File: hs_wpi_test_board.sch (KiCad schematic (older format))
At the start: 34 parts

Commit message: add power flags and no connects
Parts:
- gave numbers to parts that had none: 34
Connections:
- no-connect marks 0 -> 17

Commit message: associate footprints
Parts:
- D1, D10, D2, D3, D4, D5, D6, D7, D8, D9: footprint (none) -> LEDs:LED_D5.0mm
- Q1, Q10, Q2, Q3, Q4, Q5, Q6, Q7, Q8, Q9: footprint (none) -> TO_SOT_Packages_THT:TO-92_Inline_Narrow_Oval
- R1, R10, R11, R12, R2, R3, R4, R5, R6, R7, R8, R9: footprint (none) -> Resistors_THT:R_Axial_DIN0207_L6.3mm_D2.5mm_P10.16mm_Horizontal
- SW1: footprint (none) -> Buttons_Switches_THT:SW_PUSH-12mm

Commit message: change footprint for J1
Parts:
- J1: footprint Pin_Headers:Pin_Header_Straight_2x20 -> Pin_Headers:Pin_Header_Straight_2x20_Pitch2.54mm
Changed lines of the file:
@@
 F 0 "J1" H 5850 4950 50  0000 C CNN
 F 1 "Raspberry_Pi_2_3" H 4750 7100 50  0000 C CNN
-F 2 "Pin_Headers:Pin_Header_Straight_2x20" H 6150 7450 50  0001 C CNN
+F 2 "Pin_Headers:Pin_Header_Straight_2x20_Pitch2.54mm" H 6150 7450 50  0001 C CNN
 F 3 "" H 5200 6050 50  0001 C CNN
 	1    5150 6200

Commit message: switch J1 footprint to Connectors:IDC_Header_Straight_40pins
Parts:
- J1: footprint Pin_Headers:Pin_Header_Straight_2x20_Pitch2.54mm -> Connectors:IDC_Header_Straight_40pins
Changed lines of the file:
@@
 F 0 "J1" H 5850 4950 50  0000 C CNN
 F 1 "Raspberry_Pi_2_3" H 4750 7100 50  0000 C CNN
-F 2 "Pin_Headers:Pin_Header_Straight_2x20_Pitch2.54mm" H 6150 7450 50  0001 C CNN
+F 2 "Connectors:IDC_Header_Straight_40pins" H 6150 7450 50  0001 C CNN
 F 3 "" H 5200 6050 50  0001 C CNN
 	1    5150 6200

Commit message: switch to wider footprint for transistors
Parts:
- Q1, Q10, Q2, Q3, Q4, Q5, Q6, Q7, Q8, Q9: footprint TO_SOT_Packages_THT:TO-92_Inline_Narrow_Oval -> TO_SOT_Packages_THT:TO-92_Inline_Wide
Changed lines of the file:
@@
 F 0 "Q9" H 1950 5150 50  0000 L CNN
 F 1 "Q_NPN_EBC" H 1950 5050 50  0000 L CNN
-F 2 "TO_SOT_Packages_THT:TO-92_Inline_Narrow_Oval" H 1950 5200 50  0001 C CNN
+F 2 "TO_SOT_Packages_THT:TO-92_Inline_Wide" H 1950 5200 50  0001 C CNN
 F 3 "" H 1750 5100 50  0001 C CNN
 	1    1750 5100
@@
 F 0 "Q10" H 3200 5150 50  0000 L CNN
 F 1 "Q_NPN_EBC" H 3200 5050 50  0000 L CNN
-F 2 "TO_SOT_Packages_THT:TO-92_Inline_Narrow_Oval" H 3200 5200 50  0001 C CNN
+F 2 "TO_SOT_Packages_THT:TO-92_Inline_Wide" H 3200 5200 50  0001 C CNN
 F 3 "" H 3000 5100 50  0001 C CNN
 	1    3000 5100
@@
 F 0 "Q5" H 1950 3250 50  0000 L CNN
 F 1 "Q_NPN_EBC" H 1950 3150 50  0000 L CNN
-F 2 "TO_SOT_Packages_THT:TO-92_Inline_Narrow_Oval" H 1950 3300 50  0001 C CNN
+F 2 "TO_SOT_Packages_THT:TO-92_Inline_Wide" H 1950 3300 50  0001 C CNN
 F 3 "" H 1750 3200 50  0001 C CNN
 	1    1750 3200
@@
 F 0 "Q6" H 3200 3250 50  0000 L CNN
 F 1 "Q_NPN_EBC" H 3200 3150 50  0000 L CNN
-F 2 "TO_SOT_Packages_THT:TO-92_Inline_Narrow_Oval" H 3200 3300 50  0001 C CNN
+F 2 "TO_SOT_Packages_THT:TO-92_Inline_Wide" H 3200 3300 50  0001 C CNN
 F 3 "" H 3000 3200 50  0001 C CNN
 	1    3000 3200
@@
 F 0 "Q7" H 4450 3250 50  0000 L CNN
 F 1 "Q_NPN_EBC" H 4450 3150 50  0000 L CNN
-F 2 "TO_SOT_Packages_THT:TO-92_Inline_Narrow_Oval" H 4450 3300 50  0001 C CNN
+F 2 "TO_SOT_Packages_THT:TO-92_Inline_Wide" H 4450 3300 50  0001 C CNN
 F 3 "" H 4250 3200 50  0001 C CNN
 	1    4250 3200
@@
 F 0 "Q8" H 5700 3250 50  0000 L CNN
 F 1 "Q_NPN_EBC" H 5700 3150 50  0000 L CNN
-F 2 "TO_SOT_Packages_THT:TO-92_Inline_Narrow_Oval" H 5700 3300 50  0001 C CNN
+F 2 "TO_SOT_Packages_THT:TO-92_Inline_Wide" H 5700 3300 50  0001 C CNN
 F 3 "" H 5500 3200 50  0001 C CNN
 	1    5500 3200
@@
 F 0 "Q1" H 1950 1350 50  0000 L CNN
 F 1 "Q_NPN_EBC" H 1950 1250 50  0000 L CNN
-F 2 "TO_SOT_Packages_THT:TO-92_Inline_Narrow_Oval" H 1950 1400 50  0001 C CNN
+F 2 "TO_SOT_Packages_THT:TO-92_Inline_Wide" H 1950 1400 50  0001 C CNN
 F 3 "" H 1750 1300 50  0001 C CNN
 	1    1750 1300
@@
 F 0 "Q2" H 3200 1350 50  0000 L CNN
 F 1 "Q_NPN_EBC" H 3200 1250 50  0000 L CNN
-F 2 "TO_SOT_Packages_THT:TO-92_Inline_Narrow_Oval" H 3200 1400 50  0001 C CNN
+F 2 "TO_SOT_Packages_THT:TO-92_Inline_Wide" H 3200 1400 50  0001 C CNN
 F 3 "" H 3000 1300 50  0001 C CNN
 	1    3000 1300
@@
 F 0 "Q3" H 4450 1350 50  0000 L CNN
 F 1 "Q_NPN_EBC" H 4450 1250 50  0000 L CNN
-F 2 "TO_SOT_Packages_THT:TO-92_Inline_Narrow_Oval" H 4450 1400 50  0001 C CNN
+F 2 "TO_SOT_Packages_THT:TO-92_Inline_Wide" H 4450 1400 50  0001 C CNN
 F 3 "" H 4250 1300 50  0001 C CNN
 	1    4250 1300
@@
 F 0 "Q4" H 5700 1350 50  0000 L CNN
 F 1 "Q_NPN_EBC" H 5700 1250 50  0000 L CNN
-F 2 "TO_SOT_Packages_THT:TO-92_Inline_Narrow_Oval" H 5700 1400 50  0001 C CNN
+F 2 "TO_SOT_Packages_THT:TO-92_Inline_Wide" H 5700 1400 50  0001 C CNN
 F 3 "" H 5500 1300 50  0001 C CNN
 	1    5500 1300

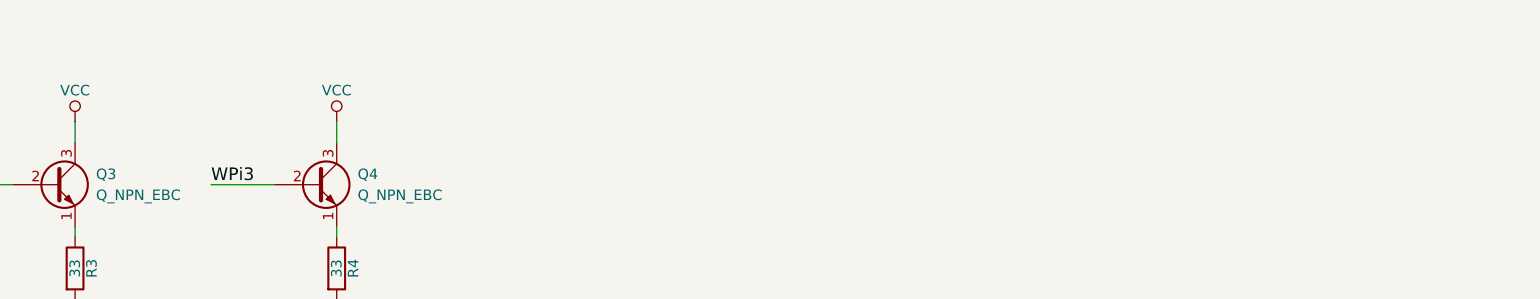
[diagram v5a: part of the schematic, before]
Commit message: add some text to schematic
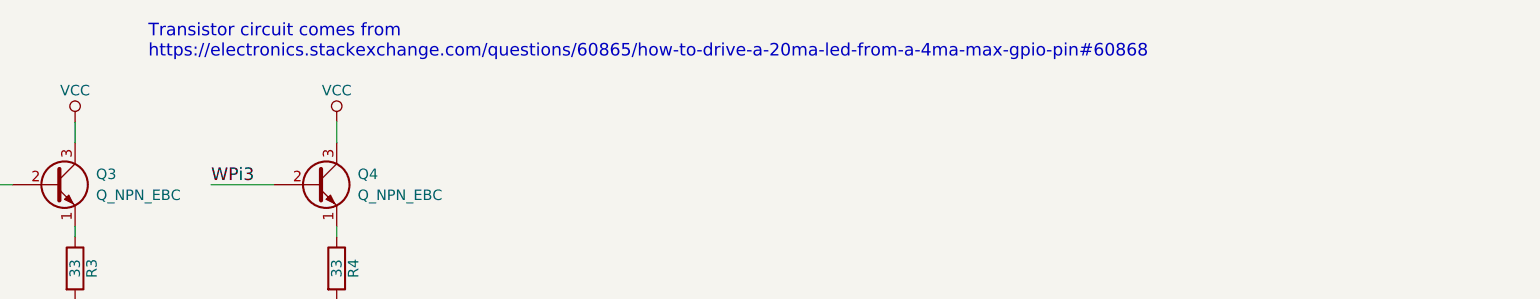
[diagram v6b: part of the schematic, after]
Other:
- note added: "Transistor circuit comes from\nhttps://electronics.stackexchange.com/questions/60865/how-to-drive-a-20ma-led-from-a-4ma-max-gpio-pin#60868"
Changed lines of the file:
@@
 encoding utf-8
 Sheet 1 1
-Title ""
-Date ""
+Title "Test board for wiringPi Haskell binding"
+Date "2017-08-08"
 Rev ""
-Comp ""
+Comp "Patrick Pelletier"
 Comment1 ""
 Comment2 ""
@@
 Connection ~ 4750 7600
 Connection ~ 4950 4850
+Text Notes 4700 700  0    60   ~ 0
+Transistor circuit comes from\nhttps://electronics.stackexchange.com/questions/60865/how-to-drive-a-20ma-led-from-a-4ma-max-gpio-pin#60868
 $EndSCHEMATC

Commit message: use new button footprint
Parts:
- SW1: footprint Buttons_Switches_THT:SW_PUSH-12mm -> hs_wpi_test_board:SW_PUSH-12mm_Wurth-430476085716
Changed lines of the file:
@@
 F 0 "SW1" H 1800 7400 50  0000 L CNN
 F 1 "SW_Push" H 1750 7240 50  0000 C CNN
-F 2 "Buttons_Switches_THT:SW_PUSH-12mm" H 1750 7500 50  0001 C CNN
+F 2 "hs_wpi_test_board:SW_PUSH-12mm_Wurth-430476085716" H 1750 7500 50  0001 C CNN
 F 3 "" H 1750 7500 50  0001 C CNN
 	1    1750 7300

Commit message: use connector footprint with notch on silkscreen
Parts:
- J1: footprint Connectors:IDC_Header_Straight_40pins -> hs_wpi_test_board:IDC_Header_Straight_40pins_key
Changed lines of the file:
@@
 F 0 "J1" H 5850 4950 50  0000 C CNN
 F 1 "Raspberry_Pi_2_3" H 4750 7100 50  0000 C CNN
-F 2 "Connectors:IDC_Header_Straight_40pins" H 6150 7450 50  0001 C CNN
+F 2 "hs_wpi_test_board:IDC_Header_Straight_40pins_key" H 6150 7450 50  0001 C CNN
 F 3 "" H 5200 6050 50  0001 C CNN
 	1    5150 6200
